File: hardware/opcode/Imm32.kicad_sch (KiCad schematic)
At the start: 8 parts, among them U23 74HC597, U24 74HC597, U25 74HC597, U26 74HC597

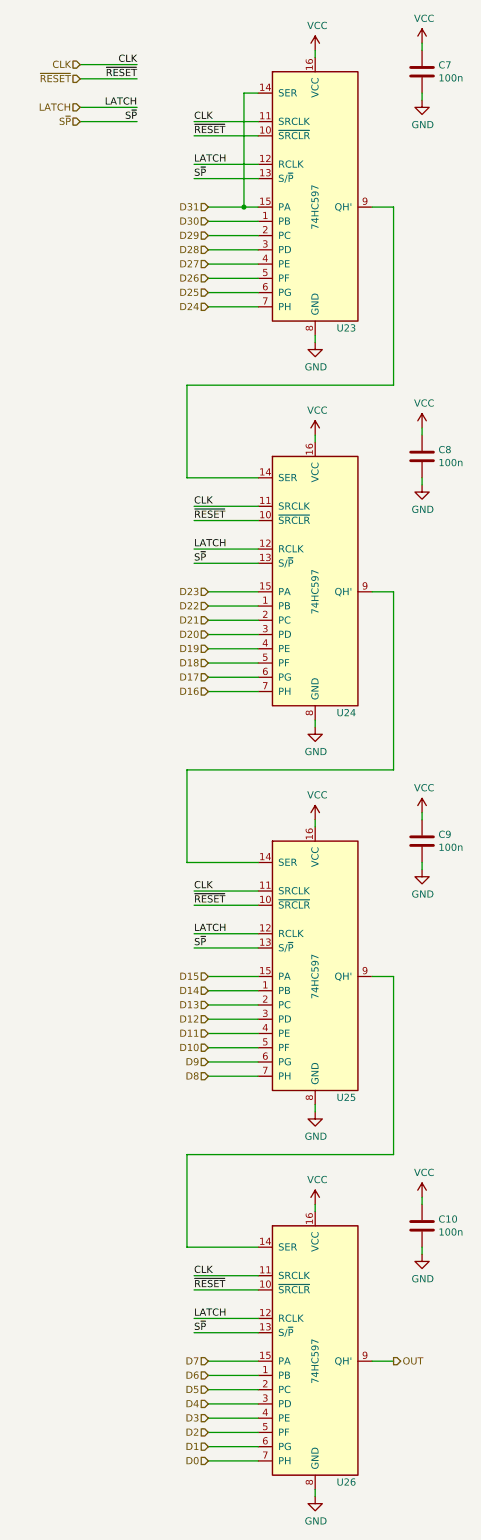
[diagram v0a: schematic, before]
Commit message: Update all to Kicad 6
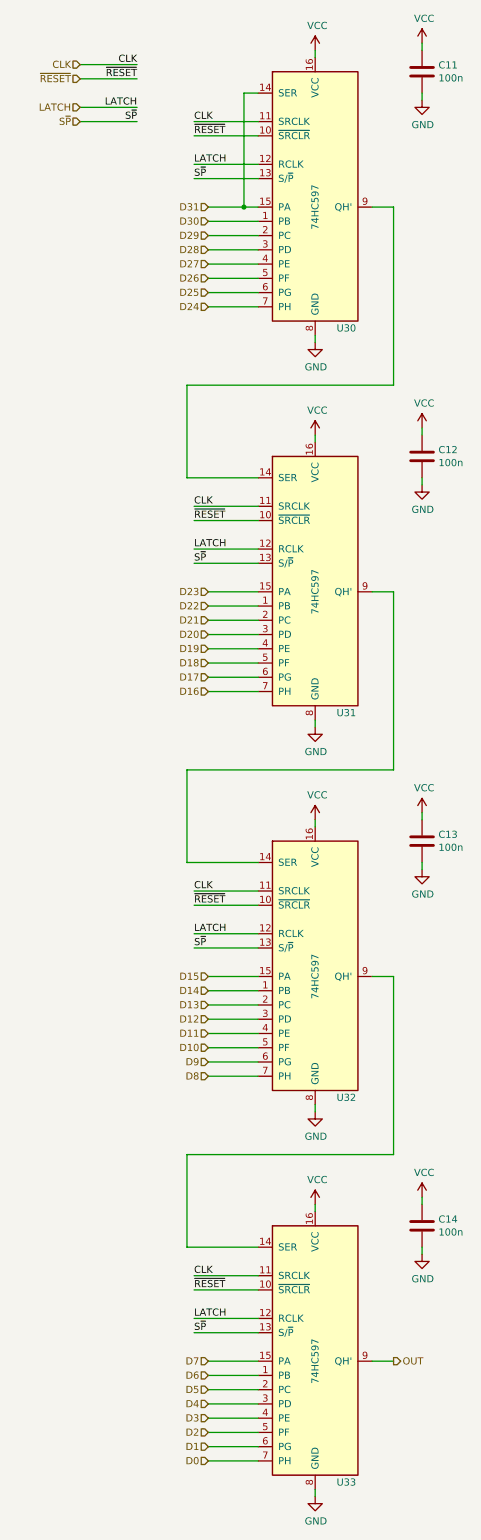
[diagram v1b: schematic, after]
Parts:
- renumbered C7 to C11, C8 to C12, C9 to C13, C10 to C14, U23 to U30, U24 to U31, U25 to U32, U26 to U33
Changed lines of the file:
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@@
   (symbol (lib_id "riscv-serial:74HC597") (at 66.04 252.73 0) (unit 1)
     (in_bom yes) (on_board yes)
-    (property "Reference" "U26" (id 0) (at 69.85 274.32 0)
+    (property "Reference" "U33" (id 0) (at 69.85 274.32 0)
       (effects (font (size 1.27 1.27)) (justify left))
     )
@@
   (symbol (lib_id "power:GND") (at 66.04 139.7 0) (unit 1)
     (in_bom yes) (on_board yes)
-    (property "Reference" "#PWR0166" (id 0) (at 66.04 146.05 0)
+    (property "Reference" "#PWR081" (id 0) (at 66.04 146.05 0)
       (effects (font (size 1.27 1.27)) hide)
     )
@@
   (symbol (lib_id "power:GND") (at 66.04 208.28 0) (unit 1)
     (in_bom yes) (on_board yes)
-    (property "Reference" "#PWR0158" (id 0) (at 66.04 214.63 0)
+    (property "Reference" "#PWR085" (id 0) (at 66.04 214.63 0)
       (effects (font (size 1.27 1.27)) hide)
     )
@@
   (symbol (lib_id "power:GND") (at 85.09 233.68 0) (unit 1)
     (in_bom yes) (on_board yes)
-    (property "Reference" "#PWR0164" (id 0) (at 85.09 240.03 0)
+    (property "Reference" "#PWR088" (id 0) (at 85.09 240.03 0)
       (effects (font (size 1.27 1.27)) hide)
     )
@@
   (symbol (lib_id "riscv-serial:74HC597") (at 66.04 184.15 0) (unit 1)
     (in_bom yes) (on_board yes)
-    (property "Reference" "U25" (id 0) (at 69.85 205.74 0)
+    (property "Reference" "U32" (id 0) (at 69.85 205.74 0)
       (effects (font (size 1.27 1.27)) (justify left))
     )
@@
   (symbol (lib_id "power:VCC") (at 66.04 156.21 0) (unit 1)
     (in_bom yes) (on_board yes)
-    (property "Reference" "#PWR0157" (id 0) (at 66.04 160.02 0)
+    (property "Reference" "#PWR083" (id 0) (at 66.04 160.02 0)
       (effects (font (size 1.27 1.27)) hide)
     )
@@
   (symbol (lib_id "Device:C") (at 85.09 160.02 0) (unit 1)
     (in_bom yes) (on_board yes)
-    (property "Reference" "C9" (id 0) (at 88.011 158.8516 0)
+    (property "Reference" "C13" (id 0) (at 88.011 158.8516 0)
       (effects (font (size 1.27 1.27)) (justify left))
     )
@@
   (symbol (lib_id "power:VCC") (at 66.04 224.79 0) (unit 1)
     (in_bom yes) (on_board yes)
-    (property "Reference" "#PWR0161" (id 0) (at 66.04 228.6 0)
+    (property "Reference" "#PWR087" (id 0) (at 66.04 228.6 0)
       (effects (font (size 1.27 1.27)) hide)
     )
@@
   (symbol (lib_id "power:GND") (at 66.04 276.86 0) (unit 1)
     (in_bom yes) (on_board yes)
-    (property "Reference" "#PWR0162" (id 0) (at 66.04 283.21 0)
+    (property "Reference" "#PWR089" (id 0) (at 66.04 283.21 0)
       (effects (font (size 1.27 1.27)) hide)
     )
@@
   (symbol (lib_id "Device:C") (at 85.09 228.6 0) (unit 1)
     (in_bom yes) (on_board yes)
-    (property "Reference" "C10" (id 0) (at 88.011 227.4316 0)
+    (property "Reference" "C14" (id 0) (at 88.011 227.4316 0)
       (effects (font (size 1.27 1.27)) (justify left))
     )
@@
   (symbol (lib_id "power:VCC") (at 85.09 223.52 0) (unit 1)
     (in_bom yes) (on_board yes)
-    (property "Reference" "#PWR0163" (id 0) (at 85.09 227.33 0)
+    (property "Reference" "#PWR086" (id 0) (at 85.09 227.33 0)
       (effects (font (size 1.27 1.27)) hide)
     )
@@
   (symbol (lib_id "riscv-serial:74HC597") (at 66.04 115.57 0) (unit 1)
     (in_bom yes) (on_board yes)
-    (property "Reference" "U24" (id 0) (at 69.85 137.16 0)
+    (property "Reference" "U31" (id 0) (at 69.85 137.16 0)
       (effects (font (size 1.27 1.27)) (justify left))
     )
@@
   (symbol (lib_id "power:VCC") (at 66.04 87.63 0) (unit 1)
     (in_bom yes) (on_board yes)
-    (property "Reference" "#PWR0165" (id 0) (at 66.04 91.44 0)
+    (property "Reference" "#PWR079" (id 0) (at 66.04 91.44 0)
       (effects (font (size 1.27 1.27)) hide)
     )
@@
   (symbol (lib_id "Device:C") (at 85.09 91.44 0) (unit 1)
     (in_bom yes) (on_board yes)
-    (property "Reference" "C8" (id 0) (at 88.011 90.2716 0)
+    (property "Reference" "C12" (id 0) (at 88.011 90.2716 0)
       (effects (font (size 1.27 1.27)) (justify left))
     )
@@
   (symbol (lib_id "power:VCC") (at 85.09 86.36 0) (unit 1)
     (in_bom yes) (on_board yes)
-    (property "Reference" "#PWR0167" (id 0) (at 85.09 90.17 0)
+    (property "Reference" "#PWR078" (id 0) (at 85.09 90.17 0)
       (effects (font (size 1.27 1.27)) hide)
     )
@@
   (symbol (lib_id "power:GND") (at 85.09 96.52 0) (unit 1)
     (in_bom yes) (on_board yes)
-    (property "Reference" "#PWR0168" (id 0) (at 85.09 102.87 0)
+    (property "Reference" "#PWR080" (id 0) (at 85.09 102.87 0)
       (effects (font (size 1.27 1.27)) hide)
     )
@@
   (symbol (lib_id "power:VCC") (at 85.09 154.94 0) (unit 1)
     (in_bom yes) (on_board yes)
-    (property "Reference" "#PWR0159" (id 0) (at 85.09 158.75 0)
+    (property "Reference" "#PWR082" (id 0) (at 85.09 158.75 0)
       (effects (font (size 1.27 1.27)) hide)
     )
@@
   (symbol (lib_id "power:GND") (at 85.09 165.1 0) (unit 1)
     (in_bom yes) (on_board yes)
-    (property "Reference" "#PWR0160" (id 0) (at 85.09 171.45 0)
+    (property "Reference" "#PWR084" (id 0) (at 85.09 171.45 0)
       (effects (font (size 1.27 1.27)) hide)
     )
@@
   (symbol (lib_id "riscv-serial:74HC597") (at 66.04 46.99 0) (unit 1)
     (in_bom yes) (on_board yes)
-    (property "Reference" "U23" (id 0) (at 69.85 68.58 0)
+    (property "Reference" "U30" (id 0) (at 69.85 68.58 0)
       (effects (font (size 1.27 1.27)) (justify left))
     )
@@
   (symbol (lib_id "power:VCC") (at 66.04 19.05 0) (unit 1)
     (in_bom yes) (on_board yes)
-    (property "Reference" "#PWR0169" (id 0) (at 66.04 22.86 0)
+    (property "Reference" "#PWR075" (id 0) (at 66.04 22.86 0)
       (effects (font (size 1.27 1.27)) hide)
     )
@@
   (symbol (lib_id "power:GND") (at 66.04 71.12 0) (unit 1)
     (in_bom yes) (on_board yes)
-    (property "Reference" "#PWR0170" (id 0) (at 66.04 77.47 0)
+    (property "Reference" "#PWR077" (id 0) (at 66.04 77.47 0)
       (effects (font (size 1.27 1.27)) hide)
     )
@@
   (symbol (lib_id "Device:C") (at 85.09 22.86 0) (unit 1)
     (in_bom yes) (on_board yes)
-    (property "Reference" "C7" (id 0) (at 88.011 21.6916 0)
+    (property "Reference" "C11" (id 0) (at 88.011 21.6916 0)
       (effects (font (size 1.27 1.27)) (justify left))
     )
@@
   (symbol (lib_id "power:VCC") (at 85.09 17.78 0) (unit 1)
     (in_bom yes) (on_board yes)
-    (property "Reference" "#PWR0171" (id 0) (at 85.09 21.59 0)
+    (property "Reference" "#PWR074" (id 0) (at 85.09 21.59 0)
       (effects (font (size 1.27 1.27)) hide)
     )
@@
   (symbol (lib_id "power:GND") (at 85.09 27.94 0) (unit 1)
     (in_bom yes) (on_board yes)
-    (property "Reference" "#PWR0172" (id 0) (at 85.09 34.29 0)
-      (effects (font (size 1.27 1.27)) hide)
-    )
+    (property "Reference" "#PWR076" (id 0) (at 85.09 34.29 0)
+      (effects (font (size 1.27 1.27)) hide)
+    )
